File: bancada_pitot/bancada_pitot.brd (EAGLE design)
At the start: 99 x 54.3 mm, 18 parts

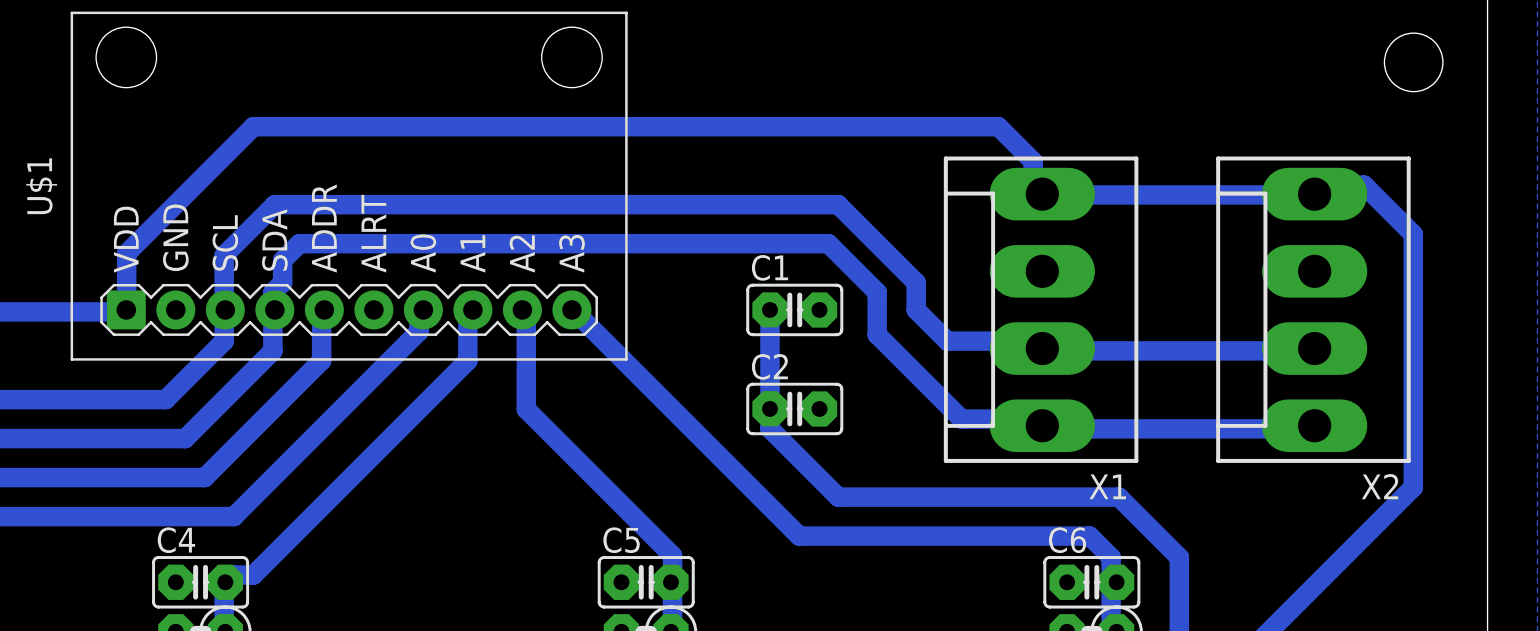
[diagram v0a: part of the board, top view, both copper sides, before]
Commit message: KK connectors changed from 4mm to 2.54mm
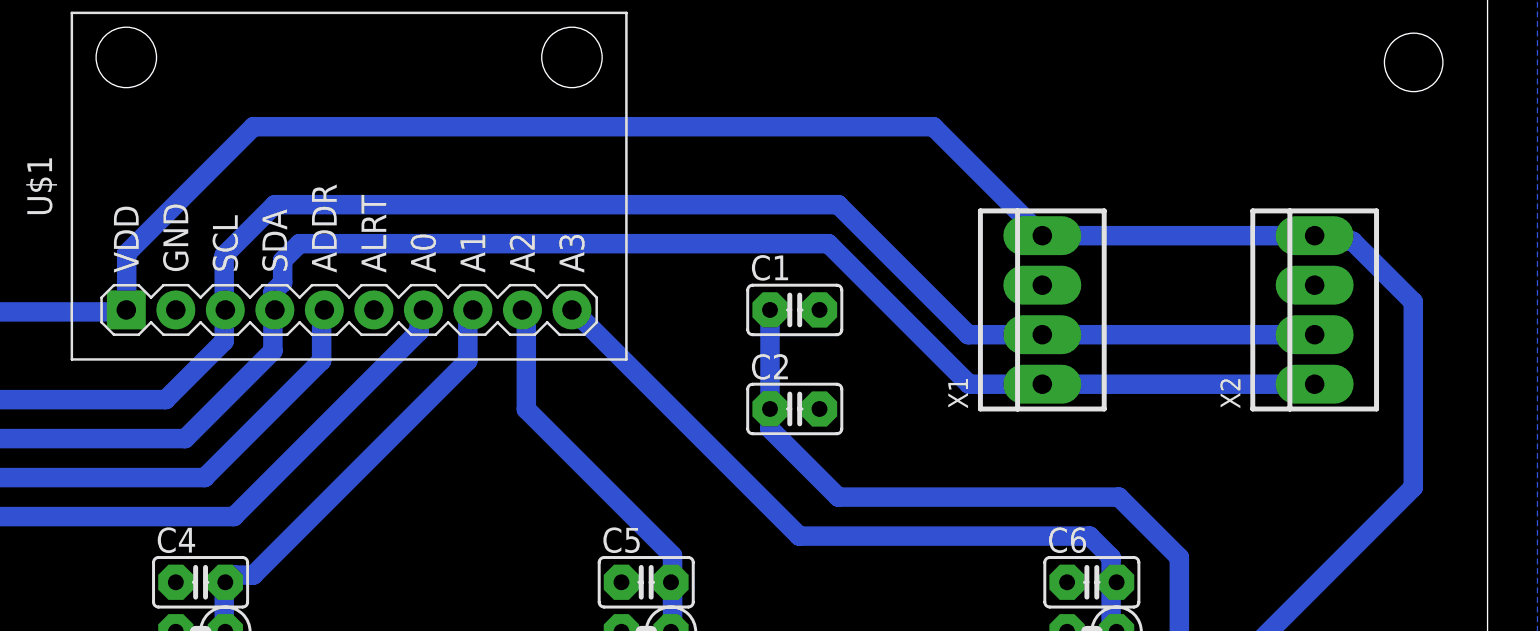
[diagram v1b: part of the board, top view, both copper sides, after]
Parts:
- X1, X2: value (none) -> 22-23-2041; device con-molex:KK-156-4 -> con-molex:22-23-2041
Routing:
- net VCC: track 276.7 -> 273.3 mm
- net SDA: track 96.2 -> 94.0 mm
- net SCL: track 90.3 -> 89.1 mm
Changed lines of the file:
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@@
 </element>
 <element name="U$1" library="diy_modules" package="ADC-4CH-ADS1115" value="ADC-4CH-ADS1115" x="40.64" y="44.45" rot="R90"/>
-<element name="X1" library="con-molex" library_urn="urn:adsk.eagle:library:165" package="KK-156-4" value="" x="76.2" y="38.1" rot="R90">
+<element name="X1" library="con-molex" library_urn="urn:adsk.eagle:library:165" package="22-23-2041" value="22-23-2041" x="76.2" y="38.1" rot="R90">
 <attribute name="MF" value="MOLEX" x="76.2" y="38.1" size="1.778" layer="27" rot="R90" display="off"/>
-<attribute name="MPN" value="" x="76.2" y="38.1" size="1.778" layer="27" rot="R90" display="off"/>
-<attribute name="OC_FARNELL" value="unknown" x="76.2" y="38.1" size="1.778" layer="27" rot="R90" display="off"/>
-<attribute name="OC_NEWARK" value="unknown" x="76.2" y="38.1" size="1.778" layer="27" rot="R90" display="off"/>
+<attribute name="MPN" value="22-23-2041" x="76.2" y="38.1" size="1.778" layer="27" rot="R90" display="off"/>
+<attribute name="OC_FARNELL" value="1462920" x="76.2" y="38.1" size="1.778" layer="27" rot="R90" display="off"/>
+<attribute name="OC_NEWARK" value="38C0355" x="76.2" y="38.1" size="1.778" layer="27" rot="R90" display="off"/>
 </element>
-<element name="X2" library="con-molex" library_urn="urn:adsk.eagle:library:165" package="KK-156-4" value="" x="90.17" y="38.1" rot="R90">
+<element name="X2" library="con-molex" library_urn="urn:adsk.eagle:library:165" package="22-23-2041" value="22-23-2041" x="90.17" y="38.1" rot="R90">
 <attribute name="MF" value="MOLEX" x="90.17" y="38.1" size="1.778" layer="27" rot="R90" display="off"/>
-<attribute name="MPN" value="" x="90.17" y="38.1" size="1.778" layer="27" rot="R90" display="off"/>
-<attribute name="OC_FARNELL" value="unknown" x="90.17" y="38.1" size="1.778" layer="27" rot="R90" display="off"/>
-<attribute name="OC_NEWARK" value="unknown" x="90.17" y="38.1" size="1.778" layer="27" rot="R90" display="off"/>
+<attribute name="MPN" value="22-23-2041" x="90.17" y="38.1" size="1.778" layer="27" rot="R90" display="off"/>
+<attribute name="OC_FARNELL" value="1462920" x="90.17" y="38.1" size="1.778" layer="27" rot="R90" display="off"/>
+<attribute name="OC_NEWARK" value="38C0355" x="90.17" y="38.1" size="1.778" layer="27" rot="R90" display="off"/>
 </element>
 <element name="JP3" library="pinhead" library_urn="urn:adsk.eagle:library:325" package="2X04" package3d_urn="urn:adsk.eagle:package:22461/2" value="" x="13.97" y="38.1" rot="R180"/>
@@
 <wire x1="28.73" y1="38" x2="29.21" y2="38.1" width="1" layer="16"/>
 <wire x1="18.23" y1="36.5" x2="17.78" y2="36.83" width="1" layer="16"/>
-<wire x1="89.73" y1="44" x2="76.23" y2="44" width="1" layer="16"/>
-<wire x1="76.23" y1="44" x2="76.2" y2="44.04" width="1" layer="16"/>
-<wire x1="89.73" y1="44" x2="90.17" y2="44.04" width="1" layer="16"/>
 <wire x1="29.23" y1="41" x2="29.23" y2="38.5" width="1" layer="16"/>
-<wire x1="35.73" y1="47.5" x2="29.23" y2="41" width="1" layer="16"/>
-<wire x1="75.73" y1="44.5" x2="75.73" y2="45.72" width="1" layer="16"/>
+<wire x1="29.23" y1="41" x2="35.73" y2="47.5" width="1" layer="16"/>
 <wire x1="29.23" y1="38.5" x2="29.21" y2="38.1" width="1" layer="16"/>
-<wire x1="75.73" y1="44.5" x2="76.2" y2="44.04" width="1" layer="16"/>
 <wire x1="62.23" y1="38.1" x2="62.23" y2="33.02" width="1" layer="16"/>
 <wire x1="25.73" y1="5.5" x2="24.13" y2="5.5" width="1" layer="16"/>
@@
 <wire x1="83.23" y1="19.05" x2="83.23" y2="25.4" width="1" layer="16"/>
 <wire x1="77.73" y1="11.5" x2="83.23" y2="17" width="1" layer="16"/>
-<wire x1="90.23" y1="44.5" x2="92.71" y2="44.5" width="1" layer="16"/>
-<wire x1="90.23" y1="44.5" x2="90.17" y2="44.04" width="1" layer="16"/>
 <wire x1="20.23" y1="5.5" x2="14.23" y2="11.5" width="1" layer="16"/>
 <wire x1="14.23" y1="11.5" x2="5.73" y2="11.5" width="1" layer="16"/>
@@
 <wire x1="83.23" y1="25.4" x2="80.13" y2="28.5" width="1" layer="16"/>
 <wire x1="80.13" y1="28.5" x2="65.73" y2="28.5" width="1" layer="16"/>
-<wire x1="92.71" y1="44.5" x2="95.23" y2="41.98" width="1" layer="16"/>
-<wire x1="95.23" y1="41.98" x2="95.23" y2="29" width="1" layer="16"/>
-<wire x1="75.73" y1="45.72" x2="73.95" y2="47.5" width="1" layer="16"/>
-<wire x1="73.95" y1="47.5" x2="35.73" y2="47.5" width="1" layer="16"/>
 <wire x1="83.23" y1="17" x2="84.55" y2="18.32" width="1" layer="16"/>
 <wire x1="84.55" y1="18.32" x2="95.23" y2="29" width="1" layer="16"/>
 <wire x1="83.23" y1="19.05" x2="83.96" y2="18.32" width="1" layer="16"/>
 <wire x1="83.96" y1="18.32" x2="84.55" y2="18.32" width="1" layer="16"/>
+<wire x1="76.2" y1="41.91" x2="90.17" y2="41.91" width="1" layer="16"/>
+<wire x1="92.10695625" y1="41.632" x2="90.448" y2="41.632" width="1" layer="16"/>
+<wire x1="90.448" y1="41.632" x2="90.17" y2="41.91" width="1" layer="16"/>
+<wire x1="95.23" y1="29" x2="95.23" y2="38.50895625" width="1" layer="16"/>
+<wire x1="95.23" y1="38.50895625" x2="92.10695625" y2="41.632" width="1" layer="16"/>
+<wire x1="35.73" y1="47.5" x2="70.61" y2="47.5" width="1" layer="16"/>
+<wire x1="70.61" y1="47.5" x2="76.2" y2="41.91" width="1" layer="16"/>
 </signal>
 <signal name="GND">
@@
 <contactref element="X2" pad="2"/>
 <contactref element="JP3" pad="6"/>
-<wire x1="89.73" y1="36" x2="76.23" y2="36" width="1" layer="16"/>
-<wire x1="76.23" y1="36" x2="76.2" y2="36.12" width="1" layer="16"/>
-<wire x1="89.73" y1="36" x2="90.17" y2="36.12" width="1" layer="16"/>
 <wire x1="34.23" y1="36.5" x2="34.23" y2="38" width="1" layer="16"/>
 <wire x1="31.23" y1="33.5" x2="34.23" y2="36.5" width="1" layer="16"/>
@@
 <wire x1="34.23" y1="38" x2="34.29" y2="38.1" width="1" layer="16"/>
 <wire x1="12.73" y1="36.5" x2="12.7" y2="36.83" width="1" layer="16"/>
-<wire x1="69.73" y1="39.5" x2="69.73" y2="38.1" width="1" layer="16"/>
-<wire x1="65.73" y1="43.5" x2="69.73" y2="39.5" width="1" layer="16"/>
 <wire x1="65.73" y1="43.5" x2="36.83" y2="43.5" width="1" layer="16"/>
-<wire x1="75.73" y1="36.5" x2="76.2" y2="36.12" width="1" layer="16"/>
 <wire x1="34.23" y1="38.5" x2="34.29" y2="38.1" width="1" layer="16"/>
-<wire x1="69.73" y1="38.1" x2="71.33" y2="36.5" width="1" layer="16"/>
-<wire x1="71.33" y1="36.5" x2="75.73" y2="36.5" width="1" layer="16"/>
 <wire x1="12.73" y1="35.56" x2="14.79" y2="33.5" width="1" layer="16"/>
 <wire x1="14.79" y1="33.5" x2="31.23" y2="33.5" width="1" layer="16"/>
 <wire x1="36.83" y1="43.5" x2="34.23" y2="40.9" width="1" layer="16"/>
 <wire x1="34.23" y1="40.9" x2="34.23" y2="38.5" width="1" layer="16"/>
+<wire x1="76.2" y1="36.83" x2="72.4" y2="36.83" width="1" layer="16"/>
+<wire x1="72.4" y1="36.83" x2="65.73" y2="43.5" width="1" layer="16"/>
+<wire x1="90.17" y1="36.83" x2="76.2" y2="36.83" width="1" layer="16"/>
 </signal>
 <signal name="SDA">
@@
 <contactref element="X2" pad="1"/>
 <contactref element="JP3" pad="8"/>
-<wire x1="89.73" y1="32" x2="76.23" y2="32" width="1" layer="16"/>
-<wire x1="76.23" y1="32" x2="76.2" y2="32.16" width="1" layer="16"/>
-<wire x1="89.73" y1="32" x2="90.17" y2="32.16" width="1" layer="16"/>
 <wire x1="36.73" y1="36" x2="36.73" y2="38" width="1" layer="16"/>
 <wire x1="32.23" y1="31.5" x2="36.73" y2="36" width="1" layer="16"/>
@@
 <wire x1="36.73" y1="38" x2="36.83" y2="38.1" width="1" layer="16"/>
 <wire x1="9.73" y1="36.5" x2="10.16" y2="36.83" width="1" layer="16"/>
-<wire x1="67.73" y1="39" x2="67.73" y2="36.83" width="1" layer="16"/>
-<wire x1="65.23" y1="41.5" x2="67.73" y2="39" width="1" layer="16"/>
 <wire x1="37.23" y1="39.5" x2="37.23" y2="40.64" width="1" layer="16"/>
 <wire x1="36.73" y1="39" x2="37.23" y2="39.5" width="1" layer="16"/>
 <wire x1="36.73" y1="38.5" x2="36.73" y2="39" width="1" layer="16"/>
-<wire x1="75.73" y1="32.5" x2="76.2" y2="32.16" width="1" layer="16"/>
 <wire x1="36.73" y1="38.5" x2="36.83" y2="38.1" width="1" layer="16"/>
-<wire x1="67.73" y1="36.83" x2="72.06" y2="32.5" width="1" layer="16"/>
-<wire x1="72.06" y1="32.5" x2="75.73" y2="32.5" width="1" layer="16"/>
 <wire x1="9.73" y1="34.29" x2="12.52" y2="31.5" width="1" layer="16"/>
 <wire x1="12.52" y1="31.5" x2="32.23" y2="31.5" width="1" layer="16"/>
 <wire x1="37.23" y1="40.64" x2="38.09" y2="41.5" width="1" layer="16"/>
-<wire x1="38.09" y1="41.5" x2="65.23" y2="41.5" width="1" layer="16"/>
+<wire x1="65.23" y1="41.5" x2="38.09" y2="41.5" width="1" layer="16"/>
+<wire x1="76.2" y1="34.29" x2="72.44" y2="34.29" width="1" layer="16"/>
+<wire x1="72.44" y1="34.29" x2="65.23" y2="41.5" width="1" layer="16"/>
+<wire x1="76.2" y1="34.29" x2="90.17" y2="34.29" width="1" layer="16"/>
 </signal>
 <signal name="ADDR">

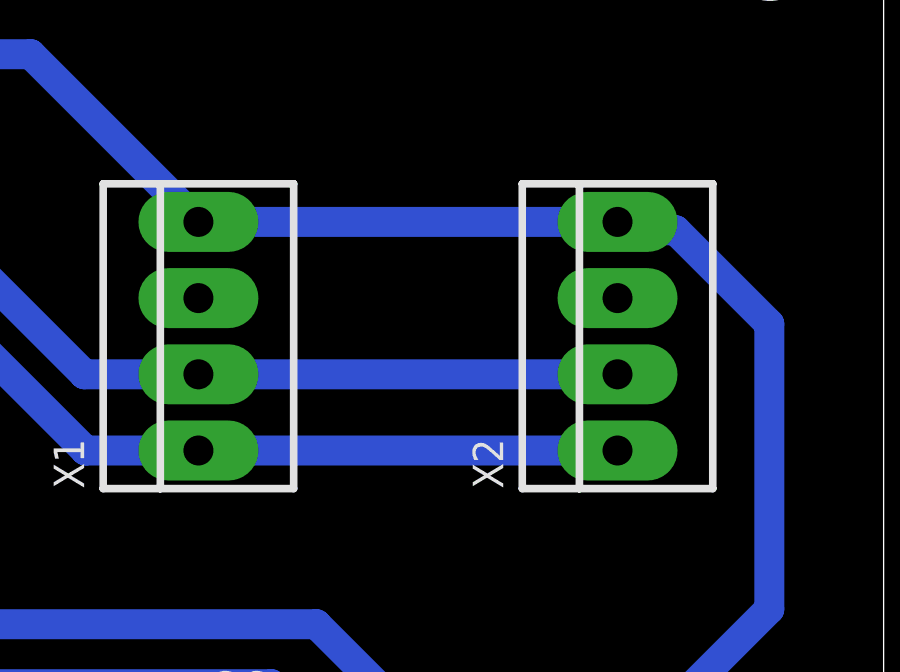
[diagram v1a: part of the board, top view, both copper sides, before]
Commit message: Increase the width of the grounded pins bridges and update DRC
The connections between the GND pins and the GND plane were too thin, so on the milling process they ended up not connected.

To solve this problem the width of those bridges were increased from 0.1016mm to 0.762mm changinf the GND polygon to 1.016mm width.

A new DRC was created as is used by both boards.
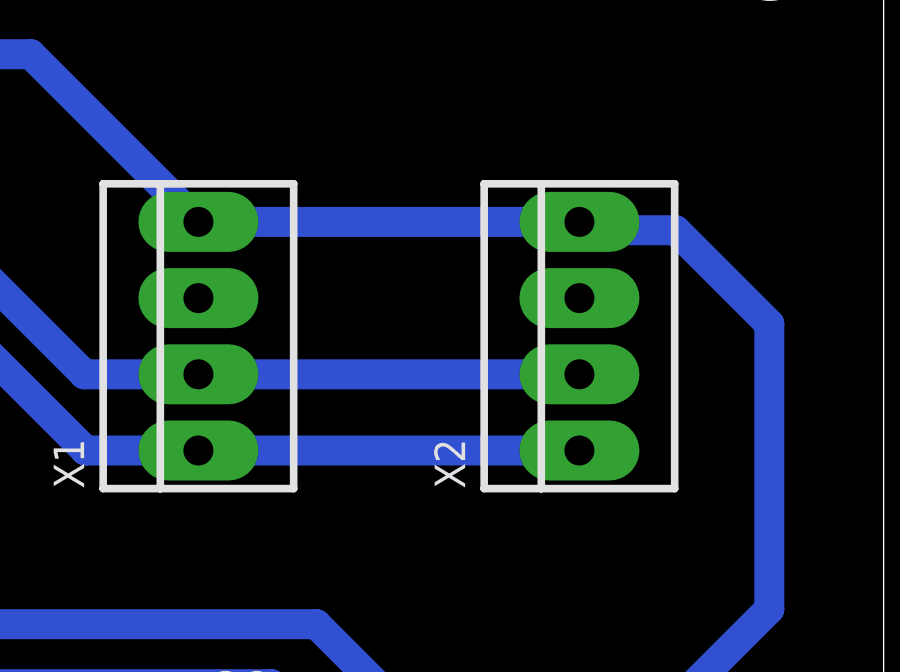
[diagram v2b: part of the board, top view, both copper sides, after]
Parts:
- moved X2 1.27 mm to (88.9, 38.1)
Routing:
- net SDA: track 94.0 -> 92.7 mm
- net SCL: track 89.1 -> 87.8 mm
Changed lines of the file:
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@@
 </class>
 </classes>
-<designrules name="regraspcb2">
+<designrules name="drc_inep">
 <description language="de">&lt;b&gt;EAGLE Design Rules&lt;/b&gt;
 &lt;p&gt;
@@
 <param name="mtCopper" value="0.035mm 0.035mm 0.035mm 0.035mm 0.035mm 0.035mm 0.035mm 0.035mm 0.035mm 0.035mm 0.035mm 0.035mm 0.035mm 0.035mm 0.035mm 0.035mm"/>
 <param name="mtIsolate" value="1.5mm 0.15mm 0.2mm 0.15mm 0.2mm 0.15mm 0.2mm 0.15mm 0.2mm 0.15mm 0.2mm 0.15mm 0.2mm 0.15mm 0.2mm"/>
-<param name="mdWireWire" value="30mil"/>
-<param name="mdWirePad" value="30mil"/>
-<param name="mdWireVia" value="30mil"/>
-<param name="mdPadPad" value="30mil"/>
-<param name="mdPadVia" value="30mil"/>
-<param name="mdViaVia" value="30mil"/>
-<param name="mdSmdPad" value="30mil"/>
-<param name="mdSmdVia" value="30mil"/>
-<param name="mdSmdSmd" value="30mil"/>
+<param name="mdWireWire" value="20mil"/>
+<param name="mdWirePad" value="20mil"/>
+<param name="mdWireVia" value="20mil"/>
+<param name="mdPadPad" value="20mil"/>
+<param name="mdPadVia" value="20mil"/>
+<param name="mdViaVia" value="20mil"/>
+<param name="mdSmdPad" value="20mil"/>
+<param name="mdSmdVia" value="20mil"/>
+<param name="mdSmdSmd" value="20mil"/>
 <param name="mdViaViaSameLayer" value="8mil"/>
 <param name="mnLayersViaInSmd" value="2"/>
-<param name="mdCopperDimension" value="0.5mm"/>
+<param name="mdCopperDimension" value="1mm"/>
 <param name="mdDrill" value="1.5mm"/>
 <param name="mdSmdStop" value="0mil"/>
-<param name="msWidth" value="1mm"/>
-<param name="msDrill" value="1mm"/>
+<param name="msWidth" value="20mil"/>
+<param name="msDrill" value="0.2mm"/>
 <param name="msMicroVia" value="9.99mm"/>
 <param name="msBlindViaRatio" value="0.5"/>
@@
 <attribute name="OC_NEWARK" value="38C0355" x="76.2" y="38.1" size="1.778" layer="27" rot="R90" display="off"/>
 </element>
-<element name="X2" library="con-molex" library_urn="urn:adsk.eagle:library:165" package="22-23-2041" value="22-23-2041" x="90.17" y="38.1" rot="R90">
-<attribute name="MF" value="MOLEX" x="90.17" y="38.1" size="1.778" layer="27" rot="R90" display="off"/>
-<attribute name="MPN" value="22-23-2041" x="90.17" y="38.1" size="1.778" layer="27" rot="R90" display="off"/>
-<attribute name="OC_FARNELL" value="1462920" x="90.17" y="38.1" size="1.778" layer="27" rot="R90" display="off"/>
-<attribute name="OC_NEWARK" value="38C0355" x="90.17" y="38.1" size="1.778" layer="27" rot="R90" display="off"/>
+<element name="X2" library="con-molex" library_urn="urn:adsk.eagle:library:165" package="22-23-2041" value="22-23-2041" x="88.9" y="38.1" rot="R90">
+<attribute name="MF" value="MOLEX" x="88.9" y="38.1" size="1.778" layer="27" rot="R90" display="off"/>
+<attribute name="MPN" value="22-23-2041" x="88.9" y="38.1" size="1.778" layer="27" rot="R90" display="off"/>
+<attribute name="OC_FARNELL" value="1462920" x="88.9" y="38.1" size="1.778" layer="27" rot="R90" display="off"/>
+<attribute name="OC_NEWARK" value="38C0355" x="88.9" y="38.1" size="1.778" layer="27" rot="R90" display="off"/>
 </element>
 <element name="JP3" library="pinhead" library_urn="urn:adsk.eagle:library:325" package="2X04" package3d_urn="urn:adsk.eagle:package:22461/2" value="" x="13.97" y="38.1" rot="R180"/>
@@
 <wire x1="83.23" y1="19.05" x2="83.96" y2="18.32" width="1" layer="16"/>
 <wire x1="83.96" y1="18.32" x2="84.55" y2="18.32" width="1" layer="16"/>
-<wire x1="76.2" y1="41.91" x2="90.17" y2="41.91" width="1" layer="16"/>
+<wire x1="76.2" y1="41.91" x2="88.9" y2="41.91" width="1" layer="16"/>
 <wire x1="92.10695625" y1="41.632" x2="90.448" y2="41.632" width="1" layer="16"/>
-<wire x1="90.448" y1="41.632" x2="90.17" y2="41.91" width="1" layer="16"/>
+<wire x1="90.448" y1="41.632" x2="88.9" y2="41.91" width="1" layer="16"/>
 <wire x1="95.23" y1="29" x2="95.23" y2="38.50895625" width="1" layer="16"/>
 <wire x1="95.23" y1="38.50895625" x2="92.10695625" y2="41.632" width="1" layer="16"/>
@@
 <contactref element="C5" pad="1"/>
 <contactref element="C6" pad="1"/>
-<polygon width="0.1524" layer="16">
+<polygon width="0.762" layer="16">
 <vertex x="-3.81" y="55.88"/>
 <vertex x="101.6" y="55.88"/>
@@
 <contactref element="X2" pad="3"/>
 <contactref element="JP3" pad="4"/>
-<wire x1="64.77" y1="33.02" x2="54.61" y2="24.13" width="0" layer="19" extent="1-1"/>
+<wire x1="54.61" y1="24.13" x2="64.77" y2="33.02" width="0" layer="19" extent="1-1"/>
 </signal>
 <signal name="A0">
@@
 <wire x1="76.2" y1="36.83" x2="72.4" y2="36.83" width="1" layer="16"/>
 <wire x1="72.4" y1="36.83" x2="65.73" y2="43.5" width="1" layer="16"/>
-<wire x1="90.17" y1="36.83" x2="76.2" y2="36.83" width="1" layer="16"/>
+<wire x1="88.9" y1="36.83" x2="76.2" y2="36.83" width="1" layer="16"/>
 </signal>
 <signal name="SDA">
@@
 <wire x1="76.2" y1="34.29" x2="72.44" y2="34.29" width="1" layer="16"/>
 <wire x1="72.44" y1="34.29" x2="65.23" y2="41.5" width="1" layer="16"/>
-<wire x1="76.2" y1="34.29" x2="90.17" y2="34.29" width="1" layer="16"/>
+<wire x1="76.2" y1="34.29" x2="88.9" y2="34.29" width="1" layer="16"/>
 </signal>
 <signal name="ADDR">
